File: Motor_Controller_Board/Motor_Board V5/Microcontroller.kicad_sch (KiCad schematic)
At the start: 21 parts, among them J301 Conn_01x04, J302 USB_B_Micro, J303 Conn_01x02, J304 Conn_01x02, J305 Conn_01x02, SW301 SW_Push, SW302 SW_Push, U301 ESP32-C6-MINI-1

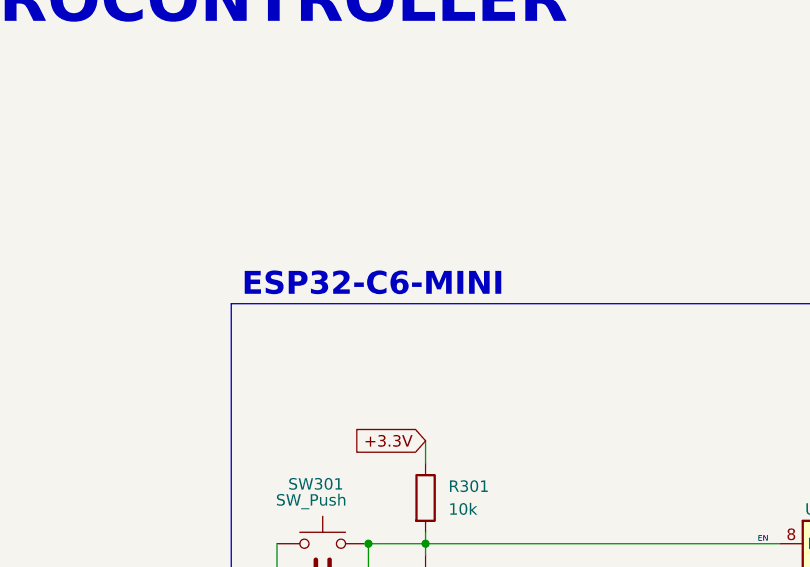
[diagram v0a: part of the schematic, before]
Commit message: cleaned up board and switched to horizontal text
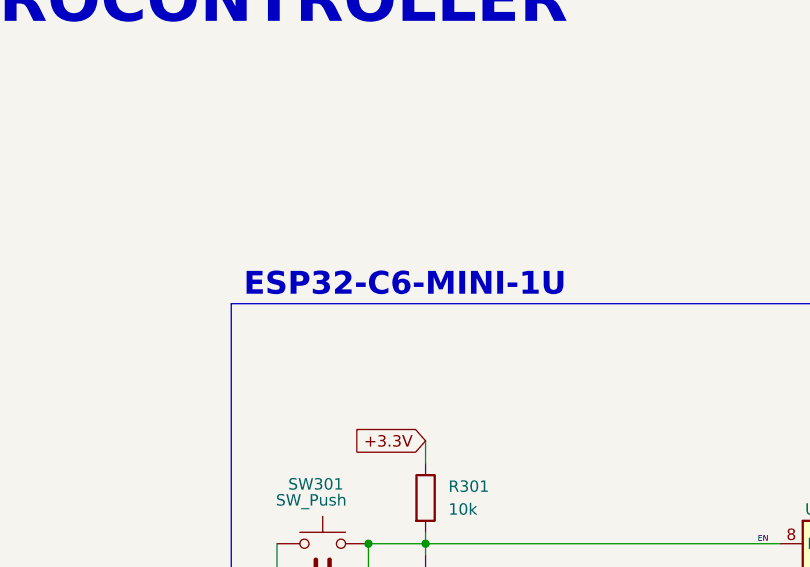
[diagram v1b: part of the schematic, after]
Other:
- note added: "ESP32-C6-MINI-1U"
- note removed: "ESP32-C6-MINI"
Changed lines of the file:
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@@
 		)
 	)
-	(text "ESP32-C6-MINI"
+	(text "ESP32-C6-MINI-1U"
 		(exclude_from_sim no)
-		(at 69.088 50.038 0)
+		(at 72.644 50.038 0)
 		(effects
 			(font
